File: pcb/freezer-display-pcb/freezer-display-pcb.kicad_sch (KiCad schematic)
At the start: 3 parts, among them J2 IT8951 board connector castel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, SW1 SW_Push, U1 ProS3

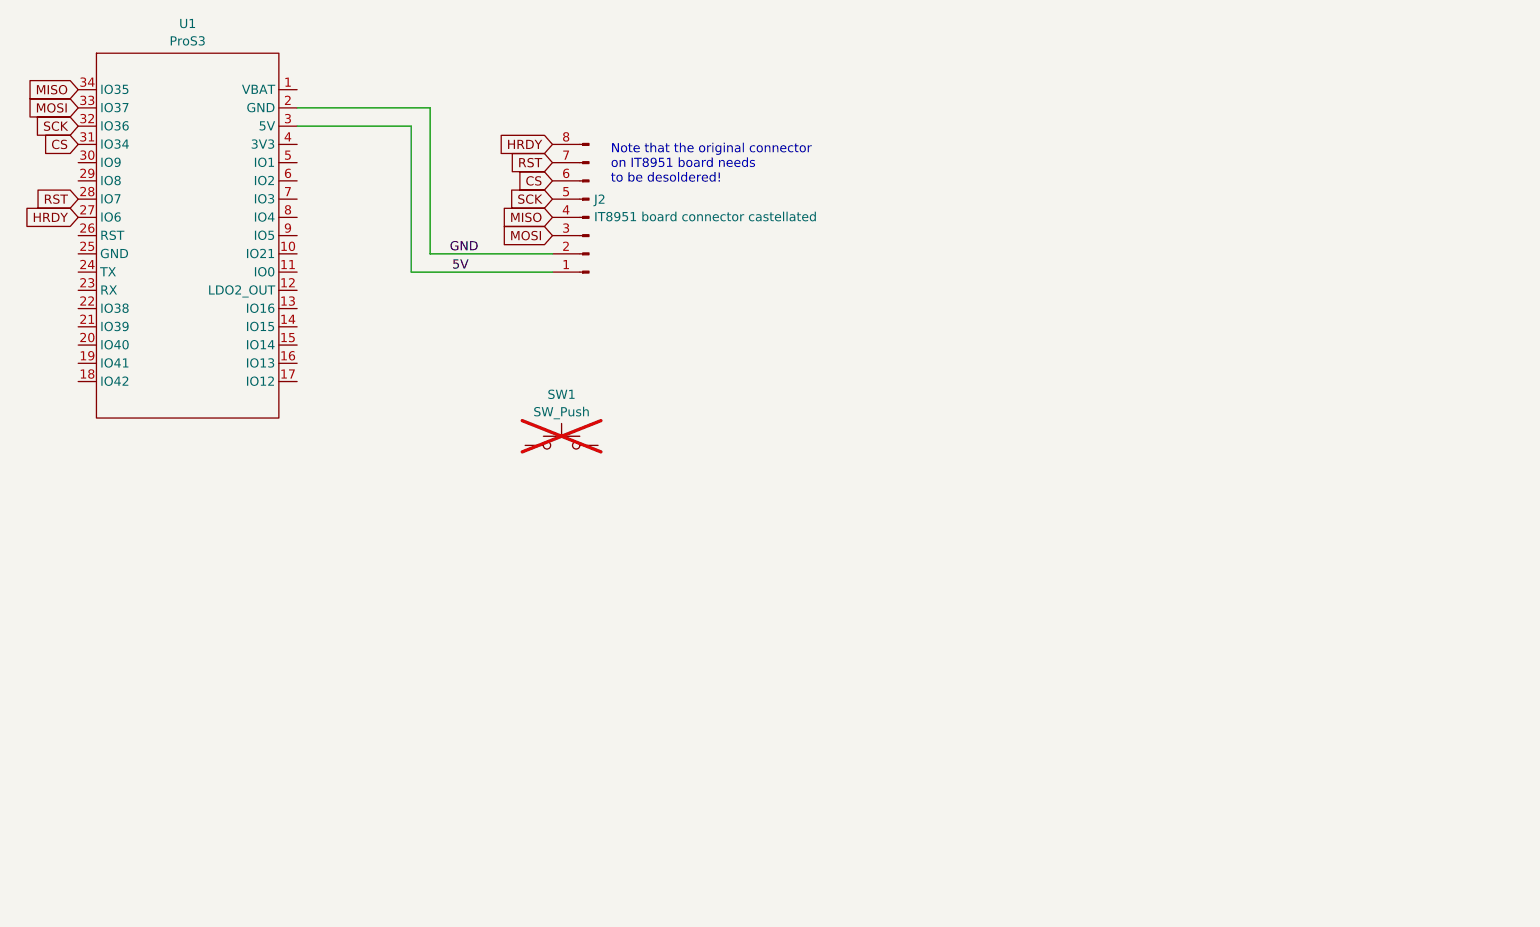
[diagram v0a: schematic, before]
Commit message: Fixed swapped net labels
MISO and MOSI nets were swapped, but the functionality of the PCB was correct. Now updated to avoid confusion. PCB design has been assembled and seems to work.  Added basic documentation for the PCB.
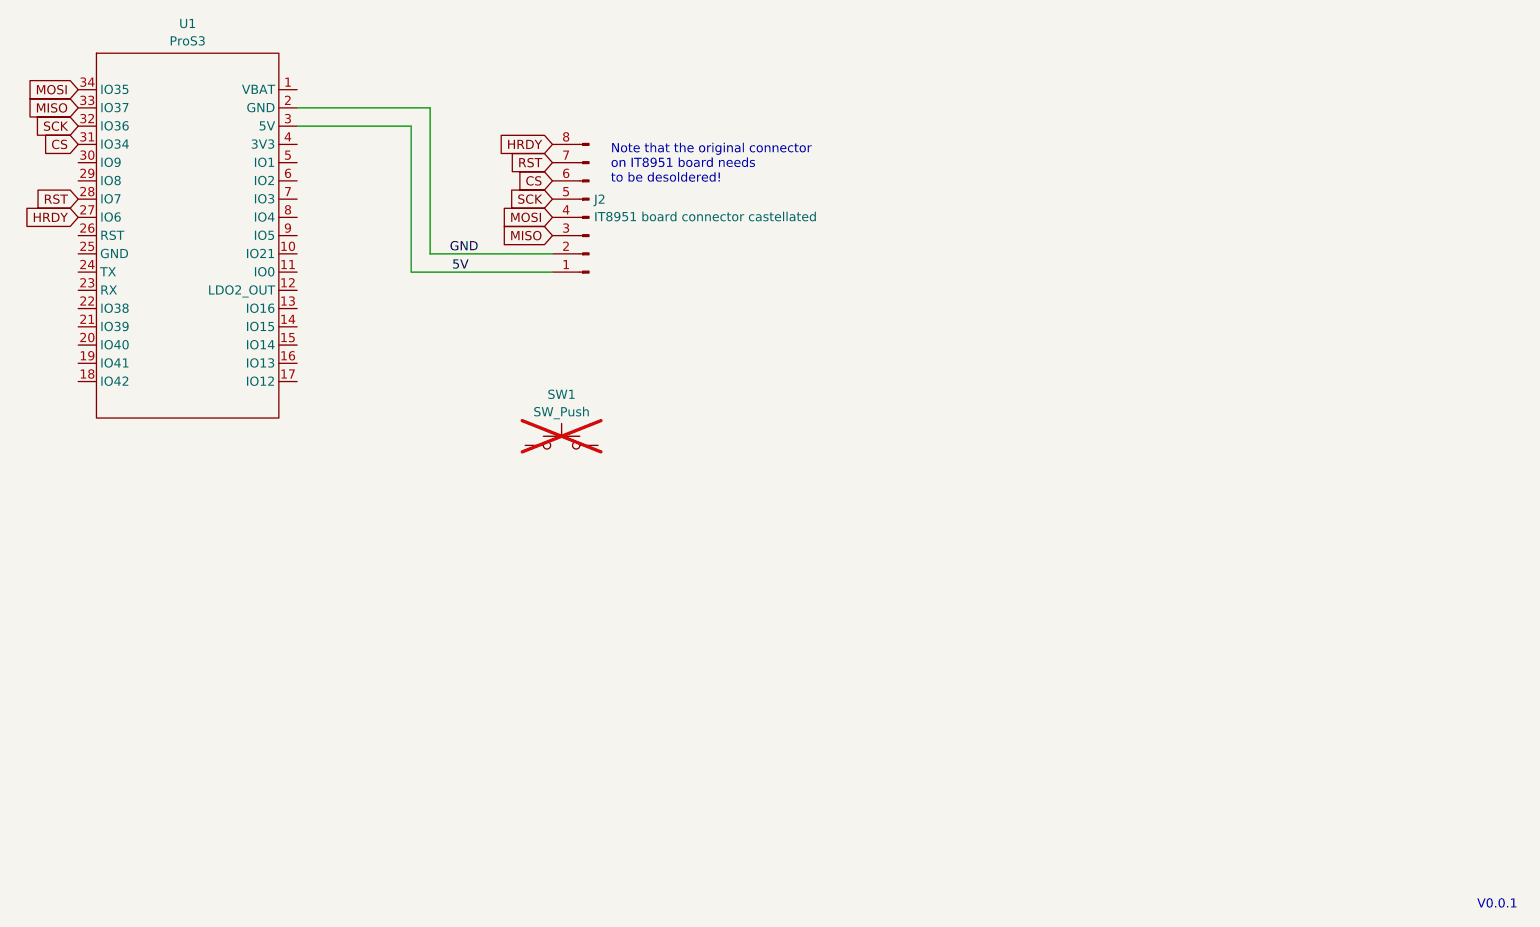
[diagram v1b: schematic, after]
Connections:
- net MISO: now also J2.3 (Pin_3), U1.33 (IO37); no longer J2.4 (Pin_4), U1.34 (IO35)
- net MOSI: now also J2.4 (Pin_4), U1.34 (IO35); no longer J2.3 (Pin_3), U1.33 (IO37)
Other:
- note added: "V0.0.1"
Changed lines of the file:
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@@
+		)
+	)
+	(text "V0.0.1"
+		(exclude_from_sim no)
+		(at 272.542 193.548 0)
+		(effects
+			(font
+				(size 1.27 1.27)
+			)
 		)
 	)
@@
 	(global_label "MOSI"
 		(shape input)
-		(at 74.93 82.55 180)
+		(at 74.93 80.01 180)
 		(fields_autoplaced yes)
 		(effects
@@
 		)
 		(property "Intersheetrefs" "${INTERSHEET_REFS}"
-			(at 67.3486 82.55 0)
+			(at 67.3486 80.01 0)
 			(effects
 				(font
@@
 	(global_label "MISO"
 		(shape input)
-		(at 140.97 97.79 180)
+		(at 140.97 100.33 180)
 		(fields_autoplaced yes)
 		(effects
@@
 		)
 		(property "Intersheetrefs" "${INTERSHEET_REFS}"
-			(at 133.3886 97.79 0)
+			(at 133.3886 100.33 0)
 			(effects
 				(font
@@
 	(global_label "MISO"
 		(shape input)
-		(at 74.93 80.01 180)
+		(at 74.93 82.55 180)
 		(fields_autoplaced yes)
 		(effects
@@
 		)
 		(property "Intersheetrefs" "${INTERSHEET_REFS}"
-			(at 67.3486 80.01 0)
+			(at 67.3486 82.55 0)
 			(effects
 				(font
@@
 	(global_label "MOSI"
 		(shape input)
-		(at 140.97 100.33 180)
+		(at 140.97 97.79 180)
 		(fields_autoplaced yes)
 		(effects
@@
 		)
 		(property "Intersheetrefs" "${INTERSHEET_REFS}"
-			(at 133.3886 100.33 0)
+			(at 133.3886 97.79 0)
 			(effects
 				(font
